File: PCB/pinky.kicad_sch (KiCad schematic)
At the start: 47 parts, among them SW10 Switch, SW11 Switch, SW12 Switch, SW13 Switch, SW14 Switch, SW15 Switch, SW16 Switch, SW17 Switch, SW18 Switch, SW2 Switch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

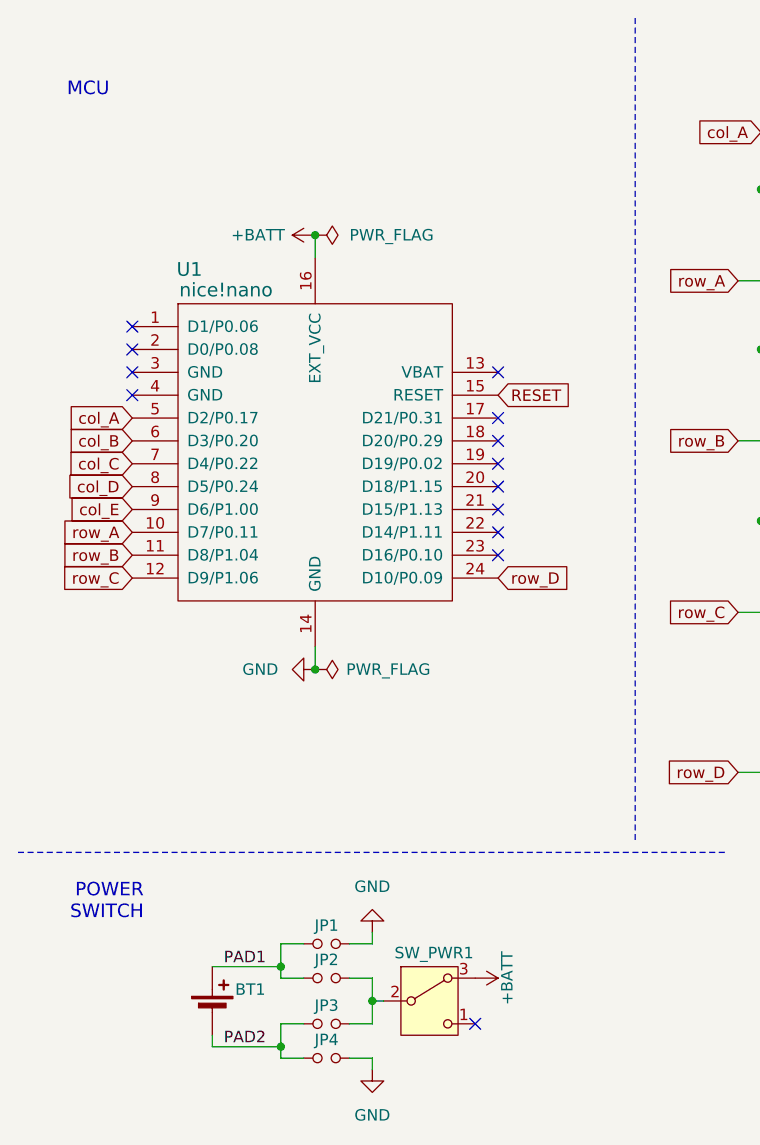
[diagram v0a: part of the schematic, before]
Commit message: Configuration jumpers for GPIO pins on the MCU
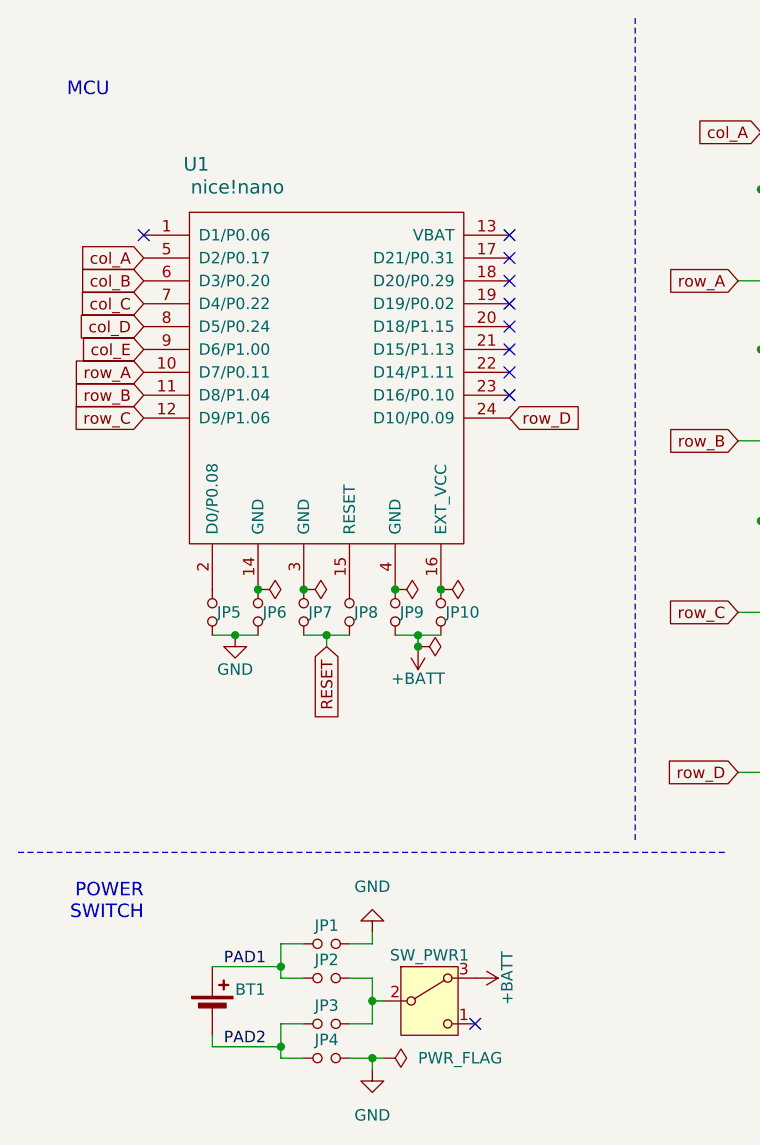
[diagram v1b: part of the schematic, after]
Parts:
- added JP10, JP5, JP6, JP7, JP8, JP9: Jumper, Pinky:Jumper, symbol Pinky:Jumper
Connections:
- net +BATT: now also JP10.1, JP9.1; no longer U1.16 (EXT_VCC)
- net GND: now also JP5.1, JP6.1; no longer U1.14 (GND)
- net RESET: now also JP7.1, JP8.1; no longer U1.15 (RESET)
- net at U1.2 (D0/P0.08): now also JP5.2
- net at U1.3 (GND): now also JP7.2
- net at U1.4 (GND): now also JP9.2
- new net: JP8.2, U1.15 (RESET)
- new net: JP10.2, U1.16 (EXT_VCC)
- new net: JP6.2, U1.14 (GND)
- no-connect marks 13 -> 10
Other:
- moved on the sheet: U1
